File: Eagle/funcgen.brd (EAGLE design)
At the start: 111.7 x 73.3 mm, 67 parts, among them IC1 AD9833, IC2 LD117ADT33TR, IC3 LM318D, IC6 LM318D, J1 DCJ0202, Q1 16MHz, Q2 ASFL1, U1 MICROCHIP_ATMEGA328PB-AUMICRO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, U3 TLV61048DBVR, X1 A1944-50

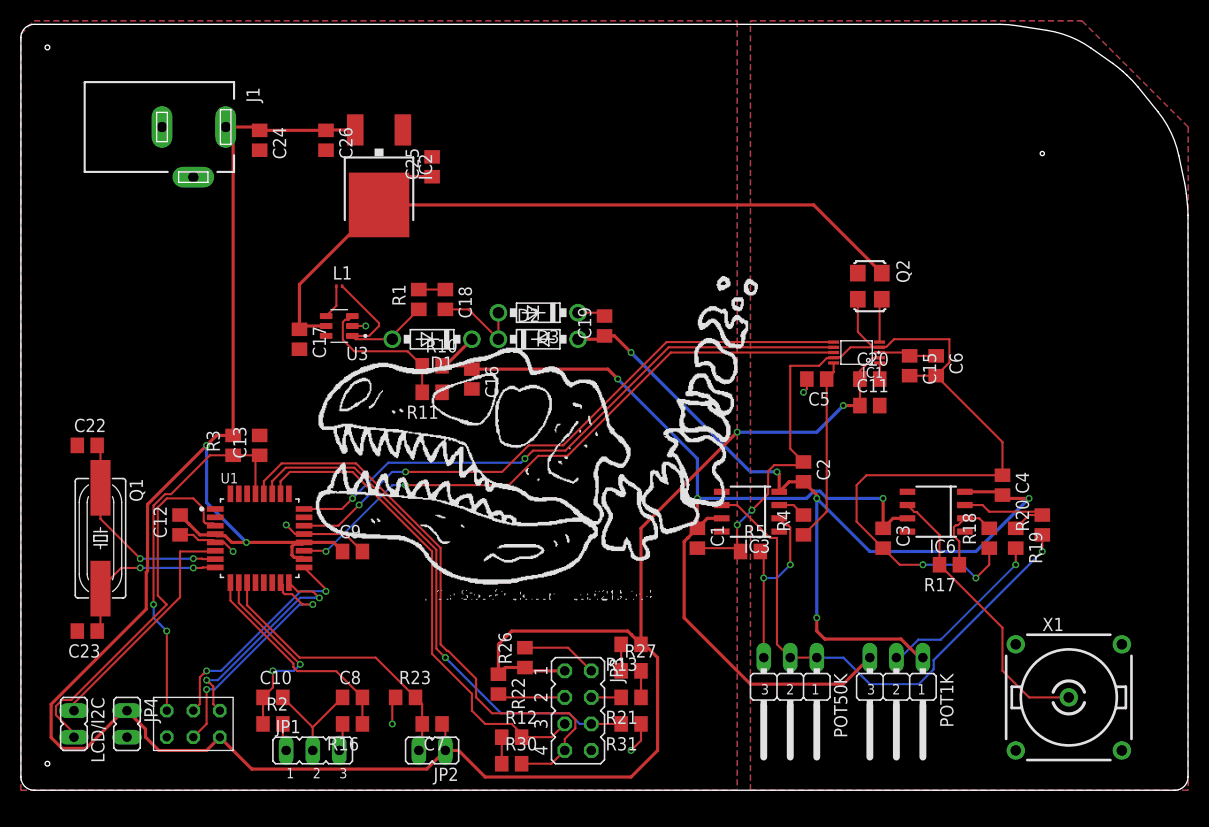
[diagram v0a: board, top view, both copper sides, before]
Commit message: Revised and Updated Schematic and Board
Changed schematic to multiple sheets with better organization. Board layout is redone entirely. Surface area is nearly cut in half from first design.
ISSUES: 1) need to verify / find the proper DC jack connector.
            2) need an 0805 inductor package. I believe I left enough space for it, but for now the footprint is entirely incorrect
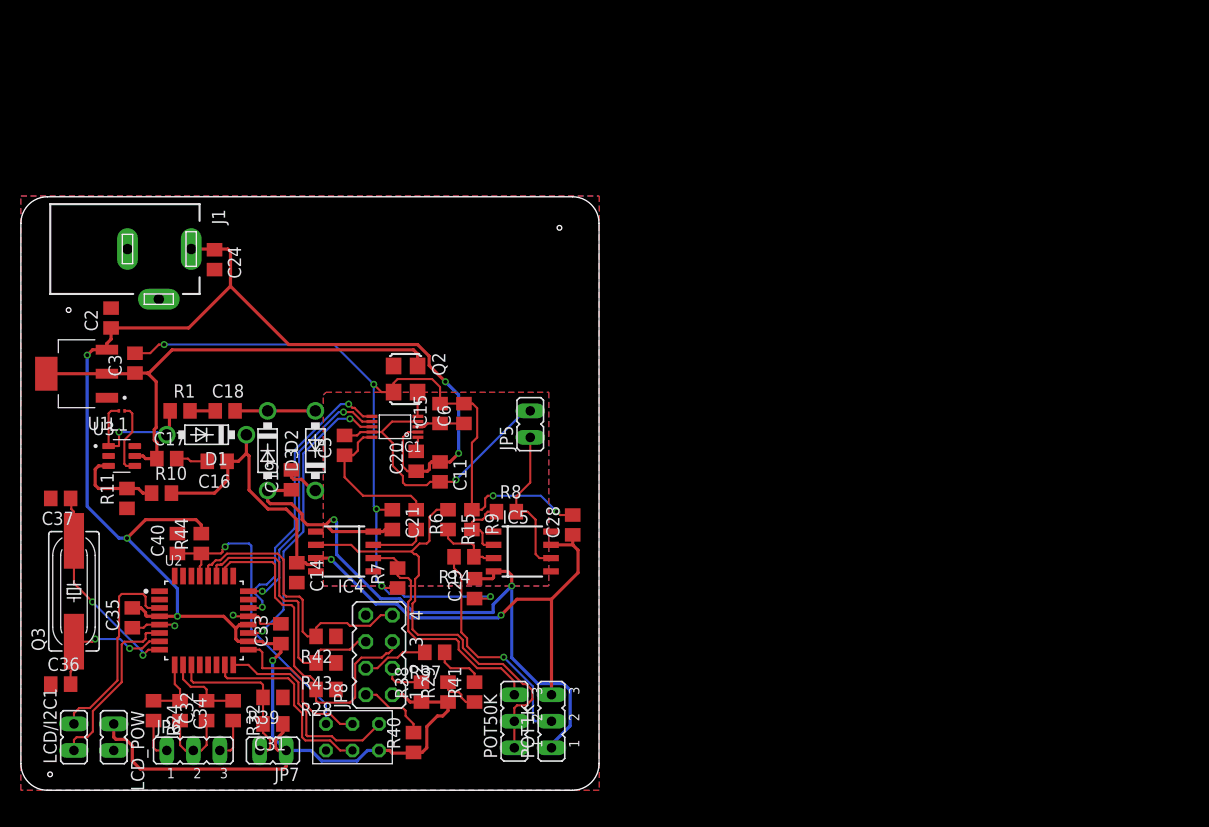
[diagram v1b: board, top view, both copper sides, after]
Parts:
- removed C1, C10, C12, C13, C26, C4, C7, C8, C9: 0.1uF, rcl:C0805
- removed C22, C23: 22pF, rcl:C0805
- removed C25: 10uF, rcl:C0805
- removed IC2: LD117ADT33TR, v-reg:DPACK
- removed IC3, IC6: LM318D, linear:SOIC8
- removed JP1: (no value), jumper:JP2
- removed JP2, JP4, LCD/I2C: (no value), jumper:JP1
- removed JP3: (no value), jumper:JP4Q
- removed Q1: 16MHz, crystal:HC49UP
- removed R12, R13, R21, R22, R23, R27, R30, R31: 1k, rcl:R0805
- removed R16, R17, R18, R19, R2, R20, R3: 10k, rcl:R0805
- removed R26: 330, rcl:R0805
- removed R4, R5: 1k3, rcl:R0805
- removed U$1: AVR-ISP, AVR-ISP:AVR-ISP
- removed X1: A1944-50, con-coax:A1944
- added C14, C21, C28, C29, C31, C32, C33, C34, C35, C40: 0.1uF, rcl:C0805
- added C36, C37: 22pF, rcl:C0805
- added IC4, IC5: LM318D, linear:SOIC8
- added JP5, JP7, LCD/I2C1, LCD_POW: (no value), jumper:JP1
- added JP6: (no value), jumper:JP2
- added JP8: (no value), jumper:JP4Q
- added Q3: 16MHz, crystal:HC49UP
- added R14, R15, R24, R32, R44, R8, R9: 10k, rcl:R0805
- added R28, R29, R37, R38, R39, R41, R42, R43: 1k, rcl:R0805
- added R40: 330, rcl:R0805
- added R6, R7: 1k3, rcl:R0805
- added U$2: AVR-ISP, AVR-ISP:AVR-ISP
- added U2: MICROCHIP_ATMEGA328PB-AUMICROCHIP_ATMEGA328PB-AU_0_0, Microchip - ATmega328PB-AU:MICROCHIP_ATMEGA328PB-AU_0
- C2, C3: value 0.1uF -> 10uF
- POT1K, POT50K: device jumper:JP2W -> jumper:JP2
- U1: value MICROCHIP_ATMEGA328PB-AUMICROCHIP_ATMEGA328PB-AU_0_0 -> TLV1117-33IDCY; device Microchip - ATmega328PB-AU:MICROCHIP_ATMEGA328PB-AU_0 -> TLV1117-33IDCY:SOT230P700X180-4N
- moved C3 73.6 mm to (10.9, 40.9), turned to 90 degrees
- moved C2 67.9 mm to (8.64, 45.2), turned to 90 degrees
- moved C5 45.7 mm to (31.0, 33.0), turned to 90 degrees
- moved C6 45.4 mm to (42.4, 36.1), turned to 90 degrees
- moved Q2 45.3 mm to (36.8, 39.4)
- moved C15 45.2 mm to (40.1, 36.1), turned to 90 degrees
- moved IC1 44.8 mm to (35.8, 34.8)
- moved C20 44.1 mm to (37.8, 31.5), turned to 90 degrees
- moved C11 41.6 mm to (40.1, 30.5), turned to 270 degrees
- moved C19 33.4 mm to (25.9, 29.7)
- moved POT1K 33.4 mm to (50.8, 6.60), turned to 90 degrees
- moved R11 30.9 mm to (10.2, 27.9), turned to 90 degrees
- moved R10 28.6 mm to (13.5, 28.4)
- moved D2 28.0 mm to (23.6, 32.5), turned to 270 degrees
- moved POT50K 26.9 mm to (47.2, 6.60), turned to 90 degrees
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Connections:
- removed net N$1: IC3.3, R4.2
- removed net N$13: JP1.1, R2.2
- removed net N$14: JP1.3, R16.2
- removed net N$15: C23.1, Q1.2, U1.8
- removed net N$16: R21.1, R27.2
- removed net N$17: R13.2, R27.1
- removed net N$18: JP3.2, R26.2
- removed net N$19: JP3.3, R22.2
- removed net N$2: IC3.2, POT50K.3, R5.2
- removed net N$20: JP3.4, R21.2
- removed net N$3: IC6.3, R19.1, R20.2
- removed net N$4: POT1K.2, R19.2
- removed net N$5: IC6.2, R17.1, R18.2
- removed net N$7: C22.2, Q1.1, U1.7
- new net N$21: IC4.3, R6.2
- new net N$22: IC4.2, POT50K.3, R7.2
- new net N$24: IC5.3, R14.1, R15.2
- new net N$25: POT1K.2, R14.2
- new net N$26: IC5.2, R8.1, R9.2
- new net N$30: JP6.1, R24.2
- new net N$31: JP6.3, R32.2
- new net N$32: C36.2, Q3.1, U2.7
- new net N$33: C37.1, Q3.2, U2.8
- new net N$34: R37.1, R41.2
- new net N$35: R29.2, R41.1
- new net N$36: JP8.2, R40.2
- new net N$37: JP8.3, R38.2
- new net N$38: JP8.4, R37.2
- net +12V: now also C14.1, C28.1, IC4.7, IC5.7; no longer C1.1, C3.1, IC3.7, IC6.7
- net +3V3: now also C3.1, U1.2, U1.4; no longer C25.1, IC2.4
- net +5V: now also C2.1, C31.1, C33.1, C35.2, JP7.1, JP8.1, LCD_POW.1, R29.1, R38.1, R40.1, R44.2, U$2.VCC, U1.3, U2.18, U2.20, U2.4; no longer C12.2, C26.1, C7.1, C9.1, IC2.3, JP2.1, JP3.1, JP4.1, R13.1, R22.1, R26.1, R3.2, U$1.VCC, U1.18, U1.20, U1.4
- net -12V: now also C21.2, C29.2, IC4.4, IC5.4; no longer C2.2, C4.2, IC3.4, IC6.4
- net A3: now also JP8.5, R28.2, U2.26; no longer JP3.5, R12.2, U1.26
- net A4: now also JP8.6, R43.2, U2.27; no longer JP3.6, R31.2, U1.27
- net A5: now also JP8.7, R42.2, U2.28; no longer JP3.7, R30.2, U1.28
- net AGND: now also IC1.4, IC1.9, JP5.2; no longer X1.2, X1.3, X1.4, X1.5
- net CS0: now also U2.14; no longer U1.14
- net CS1: now also U2.19; no longer U1.19
- net GAIN_OUT: now also IC4.6, R15.1; no longer IC3.6, R20.1
- net GND: now also C14.2, C2.2, C21.1, C28.2, C29.1, C32.1, C33.2, C34.2, C35.1, C36.1, C37.2, C40.2, JP6.2, LCD_POW.2, R28.1, R39.1, R42.1, R43.1, R7.1, R9.1, U$2.GND, U1.1, U2.21, U2.5; no longer C1.2, C10.2, C12.1, C13.2, C2.1, C22.1, C23.2, C25.2, C26.2, C4.1, C8.1, C9.2, IC1.4, IC1.9, IC2.1, JP1.2, JP4.2, R12.1, R18.1, R23.1, R30.1, R31.1, R5.1, U$1.GND, U1.21, U1.5
- net MISO0: now also U$2.MISO, U2.16; no longer U$1.MISO, U1.16
- net MOSI0: now also U$2.MOSI, U2.15; no longer U$1.MOSI, U1.15
- net MOSI1: now also U2.22; no longer U1.22
- net ROTA: now also C32.2, R32.1, U2.10; no longer C8.2, R16.1, U1.9
- net ROTB: now also C34.1, R24.1, U2.9; no longer C10.1, R2.1, U1.10
- net ROTBTN: now also C31.2, JP7.2, R39.2, U2.11; no longer C7.2, JP2.2, R23.2, U1.11
- net SCK0: now also U$2.SCK, U2.17; no longer U$1.SCK, U1.17
- net SCK1: now also U2.24; no longer U1.24
- net SCL: now also LCD/I2C1.1, U2.6; no longer LCD/I2C.1, U1.6
- net SDA: now also LCD/I2C1.2, U2.3; no longer LCD/I2C.2, U1.3
- net SIG: now also R6.1; no longer R4.1
- net SIG_OUT: now also IC5.6, JP5.1, R8.2; no longer IC6.6, R17.2, X1.1
- net UC_RST: now also C40.1, R44.1, U$2.RST, U2.29; no longer C13.1, R3.1, U$1.RST, U1.29
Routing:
- net +5V: track 258.1 -> 185.6 mm, vias 4 -> 6
- net SCK1: track 57.1 -> 25.3 mm
- net CS1: track 58.6 -> 28.3 mm
- net MOSI1: track 58.0 -> 28.3 mm
- net A5: track 56.4 -> 27.7 mm
- net AGND: track 1.40 -> 28.5 mm
- net +3V3: track 74.8 -> 48.7 mm
- net A4: track 50.9 -> 26.1 mm, vias 1 -> 0
- net N$22: track 0.00 -> 24.0 mm
- net +12V: track 95.9 -> 72.0 mm, vias 3 -> 2
- net N$25: track 0.00 -> 21.9 mm, vias 0 -> 1
- net GND: track 135.9 -> 114.8 mm
- net N$7: track 19.8 -> 0.00 mm, vias 2 -> 0
- net N$33: track 0.00 -> 19.7 mm, vias 0 -> 2
- net -12V: track 86.3 -> 67.2 mm, vias 5 -> 2
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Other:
- board size 111.7 x 73.3 mm -> 55.4 x 56.8 mm
- board text added: "Christopher Gravelle"
- board text added: "ECE 388 Fall 2020"
- board text added: "github.com/cwg19/Function-Generator"
